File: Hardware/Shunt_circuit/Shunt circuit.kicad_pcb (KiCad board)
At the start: 2 copper layers, 54.7 x 47.8 mm, 44 parts, among them U1 NXE1S0303MC, U2 INA238, U3 ISO1540, U4 ISO7710FQDRQ1

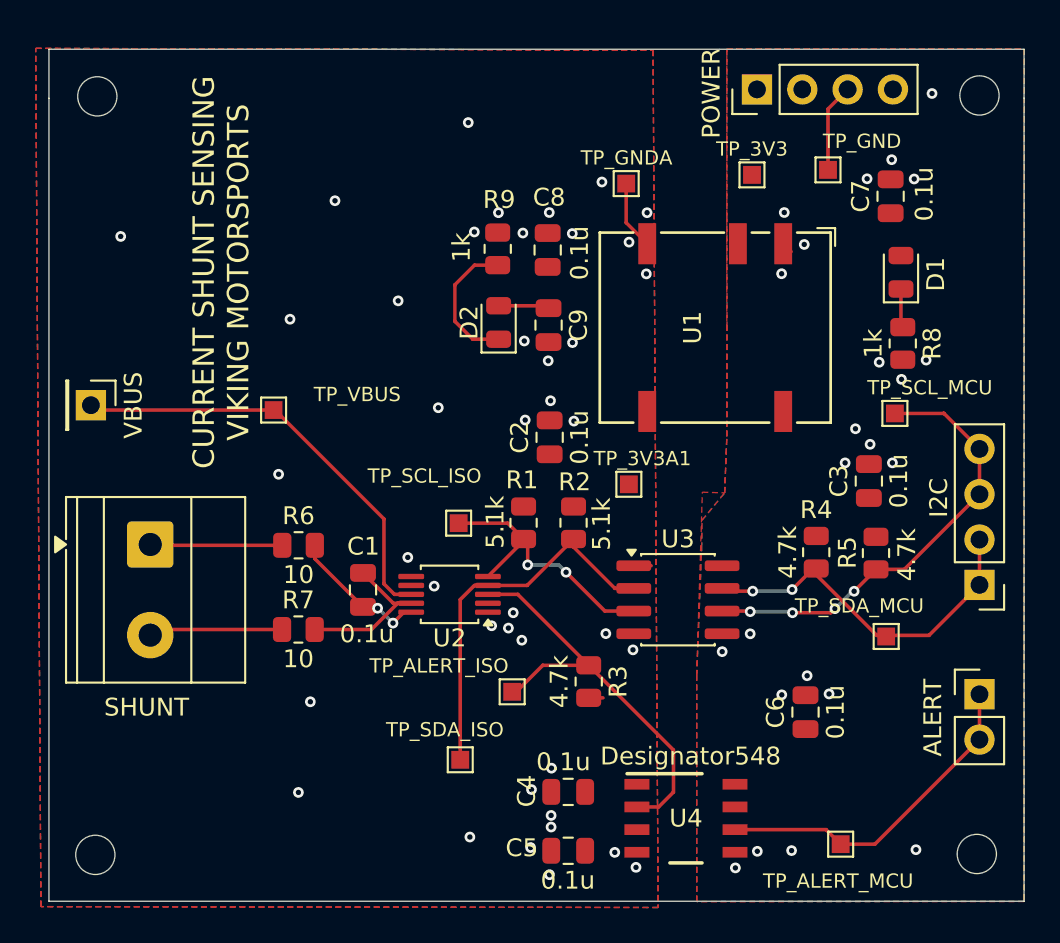
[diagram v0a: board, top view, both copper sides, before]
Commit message: Replace shunt circuit libraries and update KiCad files
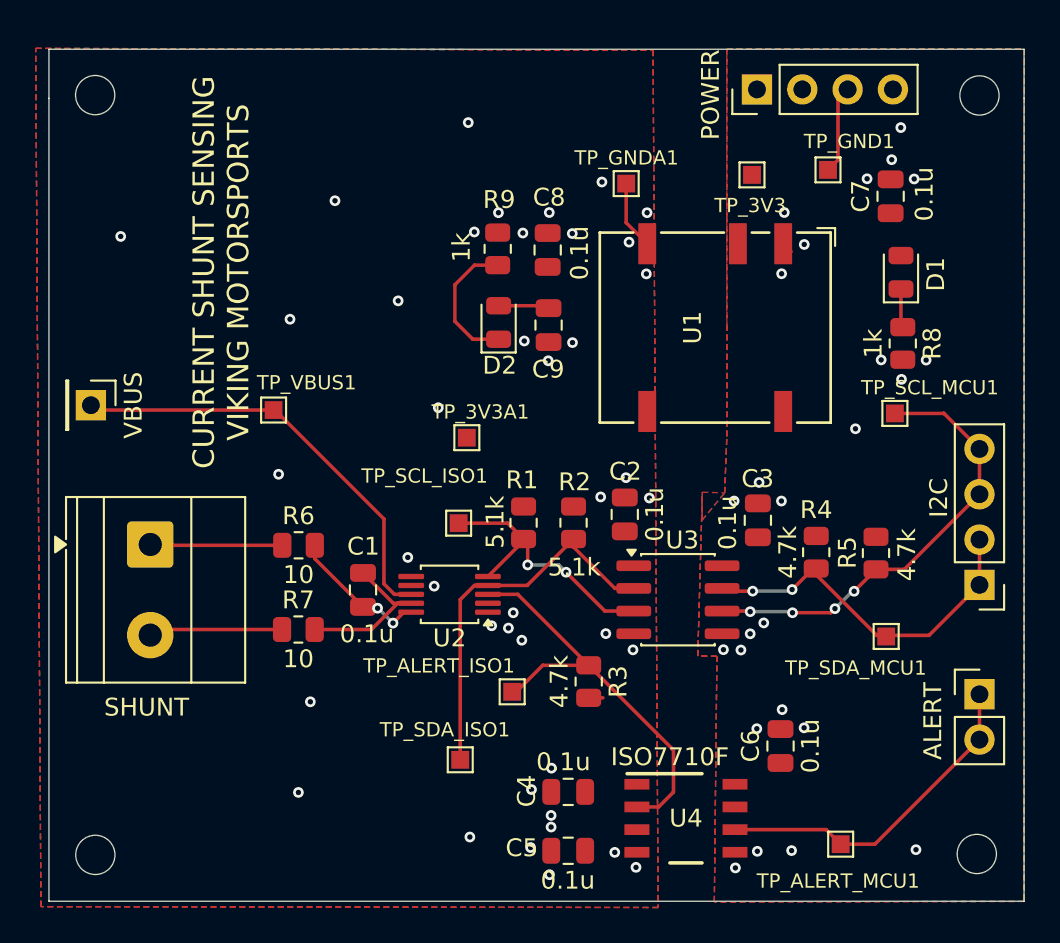
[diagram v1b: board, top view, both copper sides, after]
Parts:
- U4: footprint footprints:D0008B_HV -> footprints1:D0008B_HV
- moved TP_3V3A1 9.45 mm to (123.3, 118.8)
- moved C3 6.60 mm to (139.6, 123.4)
- moved C2 6.03 mm to (132.2, 123.1)
- moved C6 2.36 mm to (140.9, 136.1)
- moved REF** 0.14 mm to (102.5, 99.6)
- renumbered TP_ALERT_ISO to TP_ALERT_ISO1, TP_ALERT_MCU to TP_ALERT_MCU1, TP_GND to TP_GND1, TP_GNDA to TP_GNDA1, TP_SCL_ISO to TP_SCL_ISO1, TP_SCL_MCU to TP_SCL_MCU1, TP_SDA_ISO to TP_SDA_ISO1, TP_SDA_MCU to TP_SDA_MCU1, TP_VBUS to TP_VBUS1
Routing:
- net +3.3VA: track 5.78 -> 4.81 mm
- net GND: vias 23 -> 25

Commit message: Fixed shunt board, fixed .gitignore.
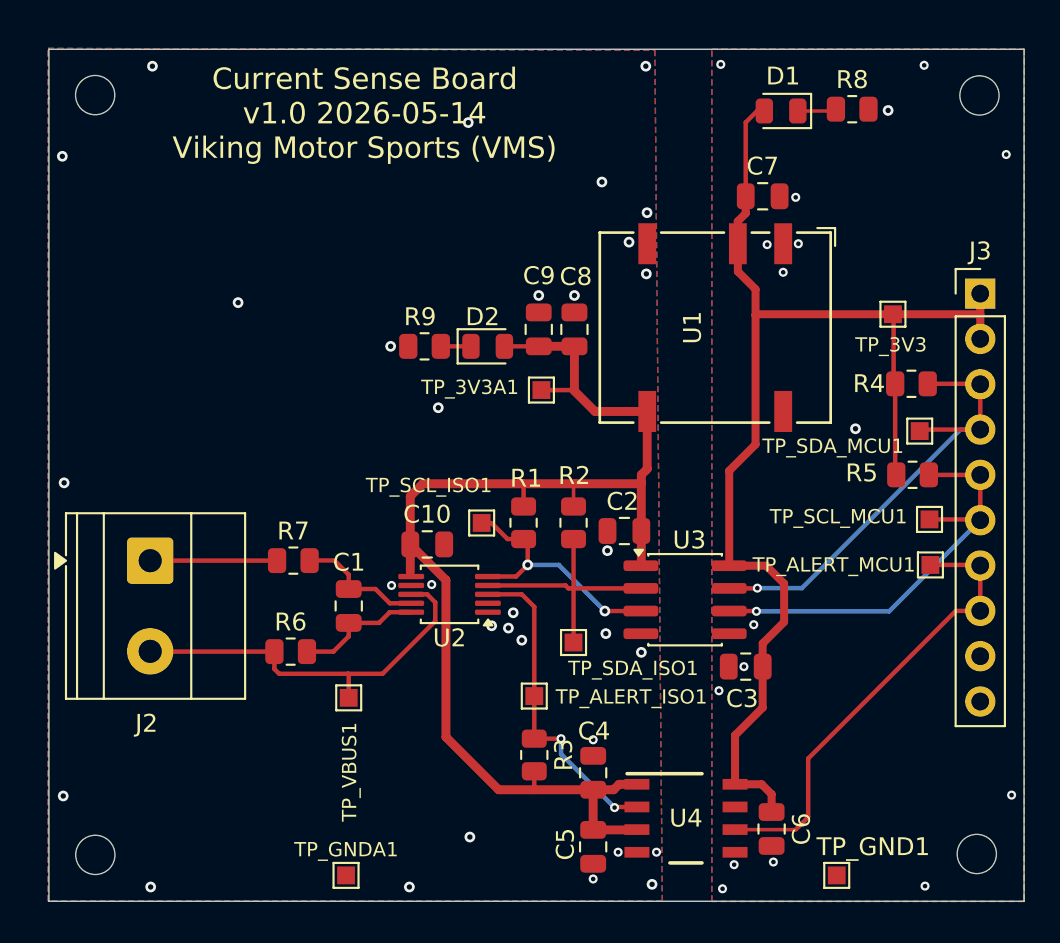
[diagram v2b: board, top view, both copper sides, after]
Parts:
- removed ALERT: ALERT CONNECTOR, Connector_PinHeader_2.54mm:PinHeader_1x02_P2.54mm_Vertical
- removed I2C: IC2 SIGNAL CONNECTOR, Connector_PinHeader_2.54mm:PinHeader_1x04_P2.54mm_Vertical
- removed POWER: POWER CONNECTOR (from the stm32), Connector_PinHeader_2.54mm:PinHeader_1x04_P2.54mm_Vertical
- removed VBUS: Vbus, Connector_PinHeader_2.54mm:PinHeader_1x01_P2.54mm_Vertical
- added C10: 0.1u, Capacitor_SMD:C_0805_2012Metric, F.Cu at (121.1, 124.8)
- added J3: Conn_01x10, Connector_PinHeader_2.54mm:PinHeader_1x10_P2.54mm_Vertical, F.Cu at (152.1, 110.7)
- D1: value PWR_LED_MCU -> GRN
- D2: value PWR_LED_ISO -> GRN
- U4: footprint footprints1:D0008B_HV -> footprints:D0008B_HV
- moved TP_GNDA1 41.8 mm to (116.5, 143.3)
- moved TP_GND1 39.5 mm to (144.1, 143.3)
- moved TP_VBUS1 16.7 mm to (116.7, 133.3)
- moved TP_ALERT_MCU1 16.4 mm to (149.3, 125.9)
- moved R8 13.4 mm to (144.9, 100.4), turned to 0 degrees
- moved TP_SDA_MCU1 11.7 mm to (148.7, 118.4)
- moved D1 11.3 mm to (140.9, 100.5), turned to 180 degrees
- moved TP_3V3 11.1 mm to (147.2, 111.8)
- moved R4 10.8 mm to (148.2, 115.8), turned to 180 degrees
- moved TP_SDA_ISO1 9.14 mm to (129.3, 130.2)
- moved C3 8.23 mm to (138.9, 131.6), turned to 180 degrees
- moved C7 7.17 mm to (139.9, 105.2), turned to 0 degrees
- moved R9 6.83 mm to (121.0, 113.7), turned to 180 degrees
- moved TP_SCL_MCU1 6.25 mm to (149.2, 123.3)
- moved R6 5.97 mm to (113.4, 130.8)
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- renumbered SHUNT to J2
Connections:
- net /ALERT_OC_BMU_GPIO renamed /ALERT
- J2 pad 1: /positive shunt input -> /-SHUNT
- J2 pad 2: /negative shunt input -> /+SHUNT
- R1 pad 1: /SCL -> +3.3VA
- R1 pad 2: +3.3VA -> /SCL
- R6 pad 1: /positive shunt input -> /+SHUNT
- R7 pad 1: /negative shunt input -> /-SHUNT
- TP_VBUS1 pad 1: /PACK+_OUT -> /+SHUNT
- U2 pad 8: /PACK+_OUT -> /+SHUNT
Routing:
- net +3.3V: track 0.07 -> 70.8 mm
- net +3.3VA: track 4.81 -> 72.2 mm
- net /PACK+_OUT: track 24.8 -> 0.00 mm
- net /+SHUNT: track 0.00 -> 22.2 mm
- net /negative shunt input: track 7.57 -> 0.00 mm
- net /positive shunt input: track 7.42 -> 0.00 mm
- net /-SHUNT: track 0.00 -> 7.11 mm
- net /SDA: track 21.5 -> 14.4 mm
- net /ALERT: track 19.0 -> 26.1 mm
- net /I2C_SDA: track 20.5 -> 26.7 mm, vias 2 -> 1
- net Net-(D2-K): track 7.77 -> 1.69 mm
- net /ALERT_OC_ISO: track 24.1 -> 18.1 mm, vias 0 -> 2
- net GND: track 5.59 -> 0.00 mm, vias 25 -> 17
- net GNDA: track 3.86 -> 0.00 mm, vias 41 -> 32
- net Net-(U2-Vin-): track 9.42 -> 7.16 mm
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- removed copper zone on F.Cu, net +3.3V
- removed copper zone on F.Cu, net +3.3VA
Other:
- board text added: "${TITLE} v${REVISION} ${ISSUE_DATE} ${COMPANY}"
- board text removed: "CURRENT SHUNT SENSING VIKING MOTORSPORTS"

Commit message: Rounded board outline
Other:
- outline, holes or cut-outs redrawn
- board text added: "${TITLE} ${COMPANY} v${REVISION} ${ISSUE_DATE}"
- board text removed: "${TITLE} v${REVISION} ${ISSUE_DATE} ${COMPANY}"
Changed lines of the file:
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@@
 		)
 	)
-	(gr_line
+	(gr_rect
 		(start 99.9 97)
-		(end 99.9 99.75)
+		(end 154.55 144.75)
+		(radius 1)
 		(stroke
 			(width 0.05)
-			(type default)
+			(type solid)
 		)
+		(fill no)
+		(locked yes)
 		(layer "Edge.Cuts")
 	)
-	(gr_line
-		(start 99.9 144.75)
-		(end 99.9 99.75)
-		(stroke
-			(width 0.05)
-			(type default)
-		)
-		(layer "Edge.Cuts")
-	)
-	(gr_line
-		(start 154.55 97)
-		(end 99.9 97)
-		(stroke
-			(width 0.05)
-			(type default)
-		)
-		(layer "Edge.Cuts")
-	)
-	(gr_line
-		(start 154.55 99.75)
-		(end 154.55 97)
-		(stroke
-			(width 0.05)
-			(type default)
-		)
-		(layer "Edge.Cuts")
-	)
-	(gr_line
-		(start 154.55 99.75)
-		(end 154.55 144.75)
-		(stroke
-			(width 0.05)
-			(type default)
-		)
-		(layer "Edge.Cuts")
-	)
-	(gr_line
-		(start 154.55 144.75)
-		(end 99.9 144.75)
-		(stroke
-			(width 0.05)
-			(type default)
-		)
-		(layer "Edge.Cuts")
-	)
-	(gr_text "${TITLE}\nv${REVISION} ${ISSUE_DATE}\n${COMPANY}"
+	(gr_text "${TITLE}\n${COMPANY}\nv${REVISION} ${ISSUE_DATE}\n"
 		(at 117.6 100.6 0)
 		(layer "F.SilkS")

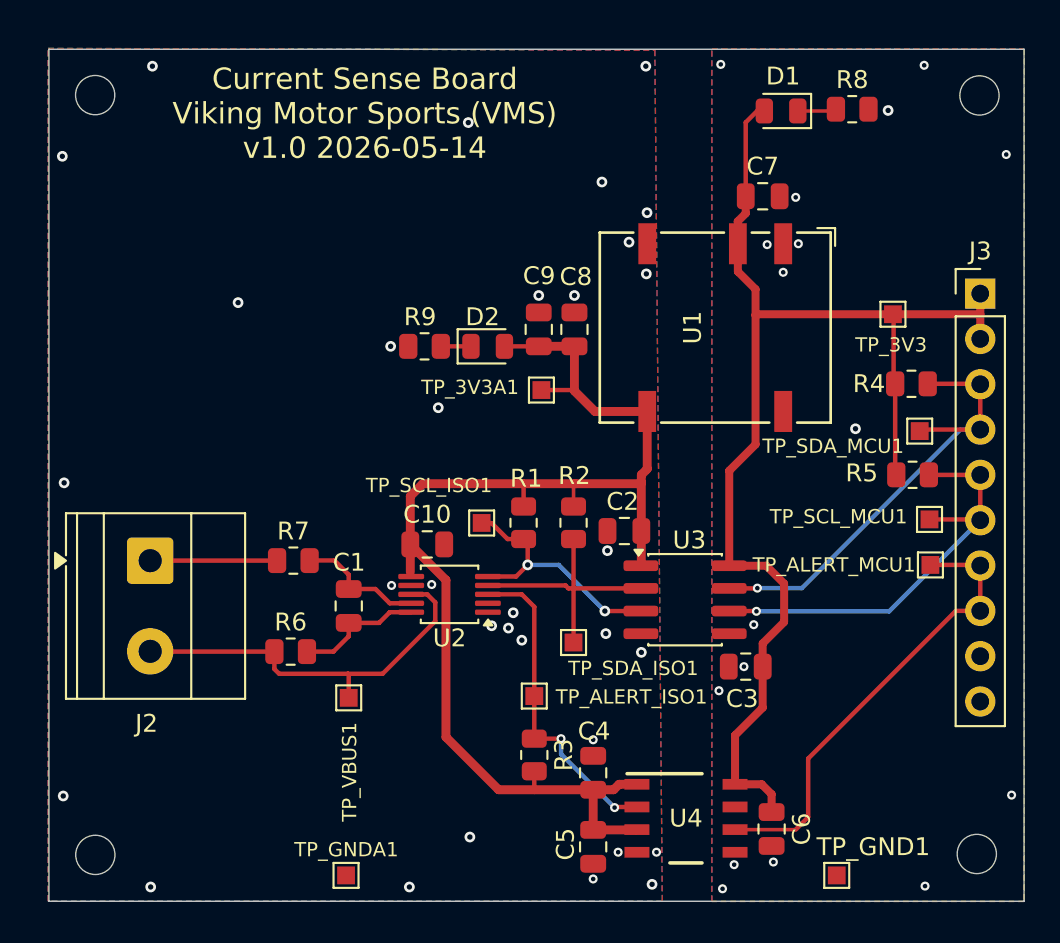
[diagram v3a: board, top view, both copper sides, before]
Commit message: doubled up pin for bmu
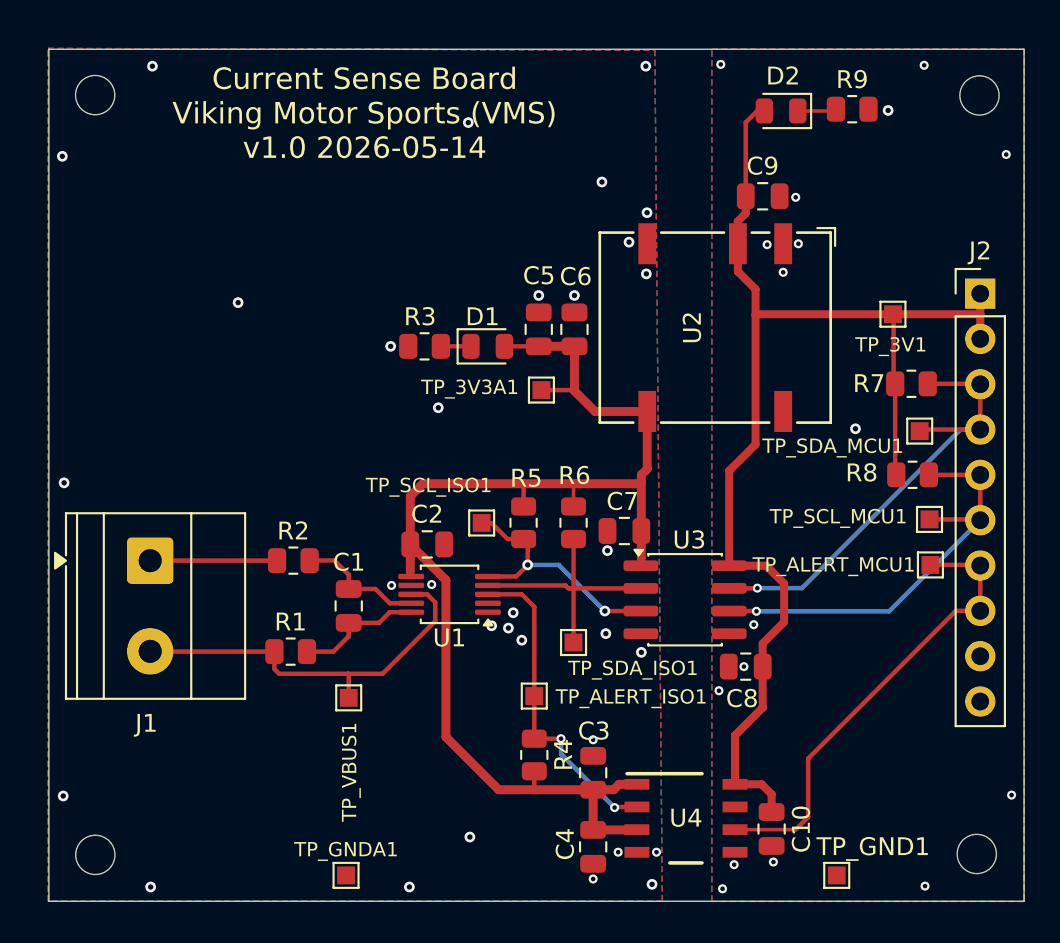
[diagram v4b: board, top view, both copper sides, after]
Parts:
- renumbered C6 to C10, C10 to C2, C4 to C3, C5 to C4, C9 to C5, C8 to C6, C2 to C7, C3 to C8, C7 to C9, D2 to D1, D1 to D2, J2 to J1, J3 to J2, R6 to R1, R7 to R2, R9 to R3, R3 to R4, R1 to R5, R2 to R6, R4 to R7, R5 to R8, R8 to R9, TP_3V3 to TP_3V1, U2 to U1, U1 to U2

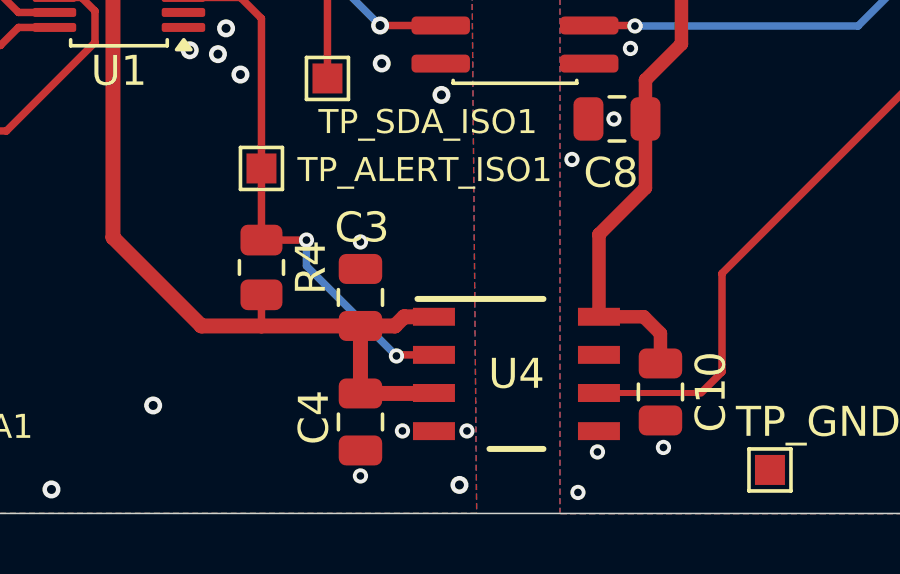
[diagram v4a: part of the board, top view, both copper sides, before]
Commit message: Made a nicer symbol, cleaned up ERC, cleaned up DRC, fabricated
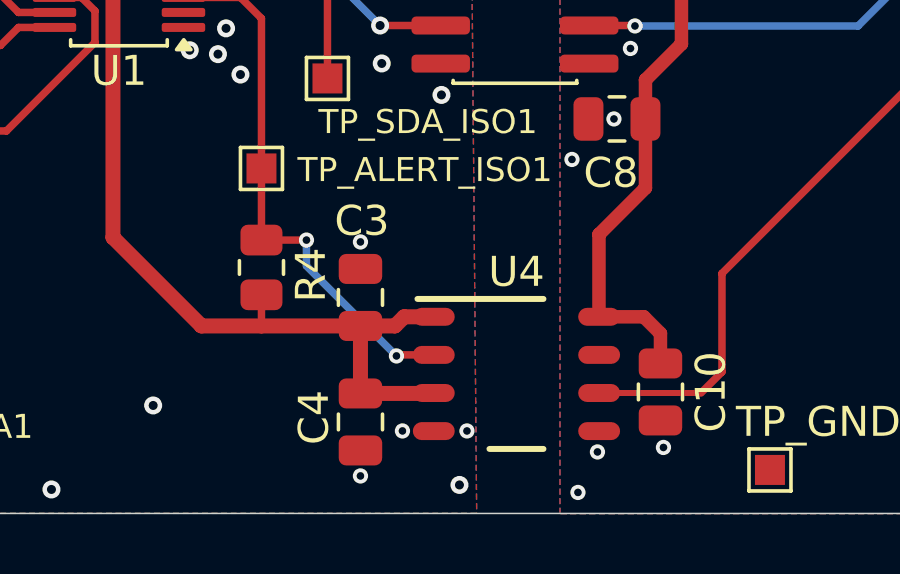
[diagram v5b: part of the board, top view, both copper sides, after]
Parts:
- U4: footprint footprints:D0008B_HV -> footprints:D0008B_N
